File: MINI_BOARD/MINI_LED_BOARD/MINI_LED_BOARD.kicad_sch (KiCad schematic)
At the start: 38 parts, among them J1 Conn_ARM_SWD_TagConnect_TC2030, J2 430450428, U1 MSPM0C1103SDDFR, U2 TCAN334, U4 TPS76333DBVR

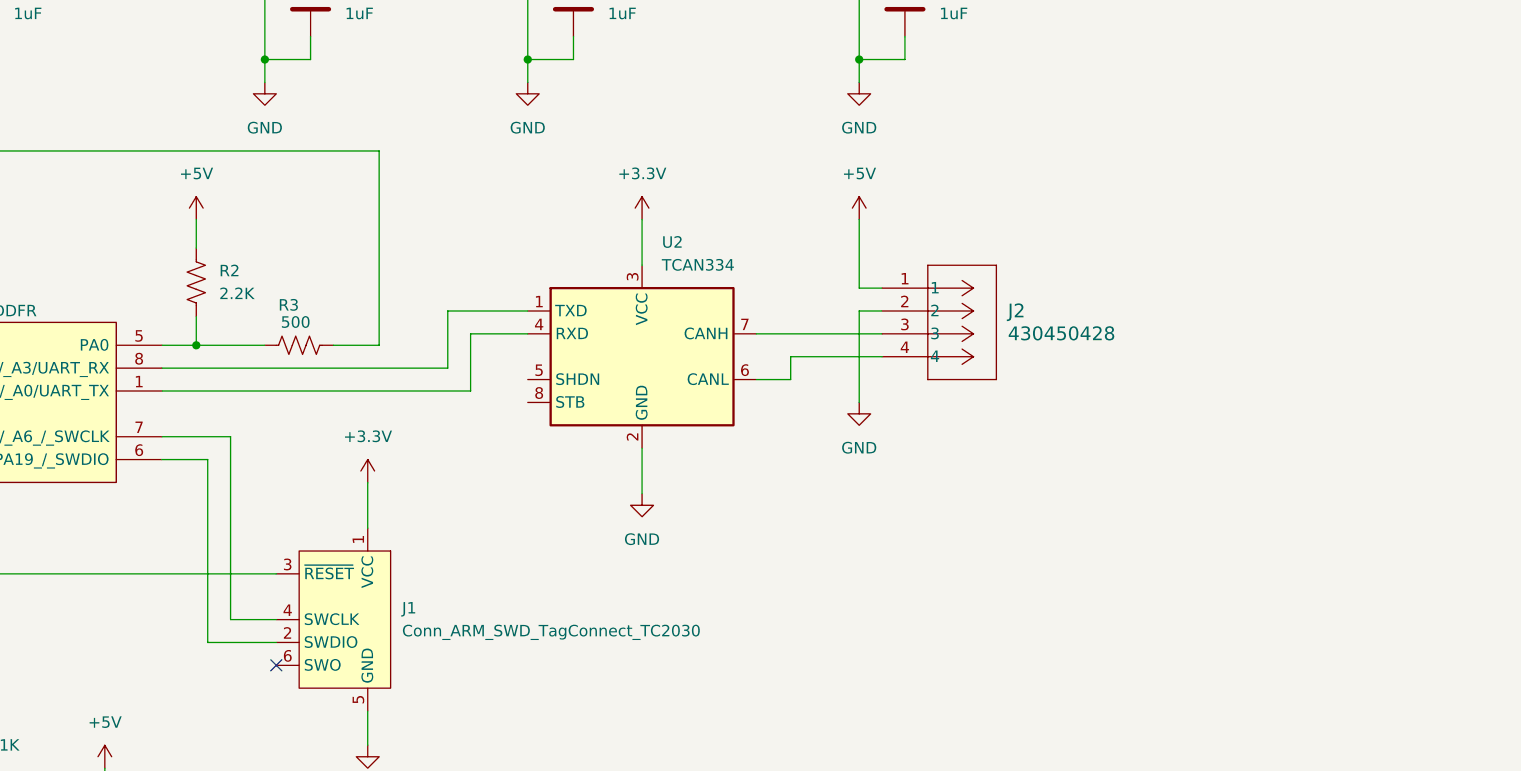
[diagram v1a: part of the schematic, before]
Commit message: Add more TCAN passives and mess with layout
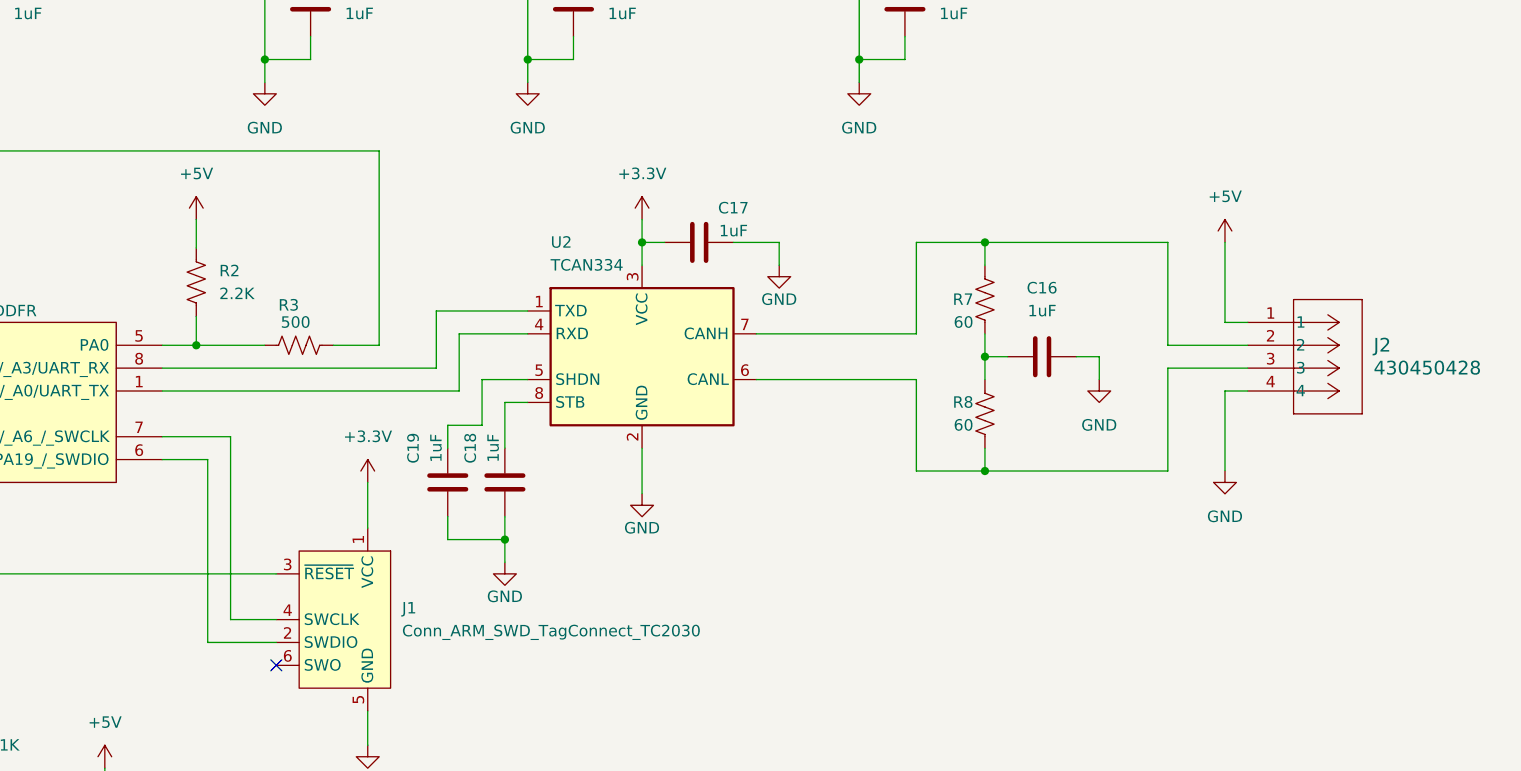
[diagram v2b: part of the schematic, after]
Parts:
- added C16, C17, C18, C19: 1uF, Capacitor_SMD:C_0603_1608Metric_Pad1.08x0.95mm_HandSolder, symbol Device:C
- added R7, R8: 60, Resistor_SMD:R_0603_1608Metric_Pad0.98x0.95mm_HandSolder, symbol Device:R_US
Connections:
- net +3.3V: now also C17.2
- net GND: now also J2.4, C16.2, C17.1, C18.2, C19.2; no longer J2.2
- net at U2.7 (CANH): now also J2.2, R7.2; no longer J2.3
- net at U2.6 (CANL): now also J2.3, R8.1; no longer J2.4
- net at U2.5 (SHDN): now also C19.1
- net at U2.8 (STB): now also C18.1
- new net: C16.1, R7.1, R8.2
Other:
- moved on the sheet: J2

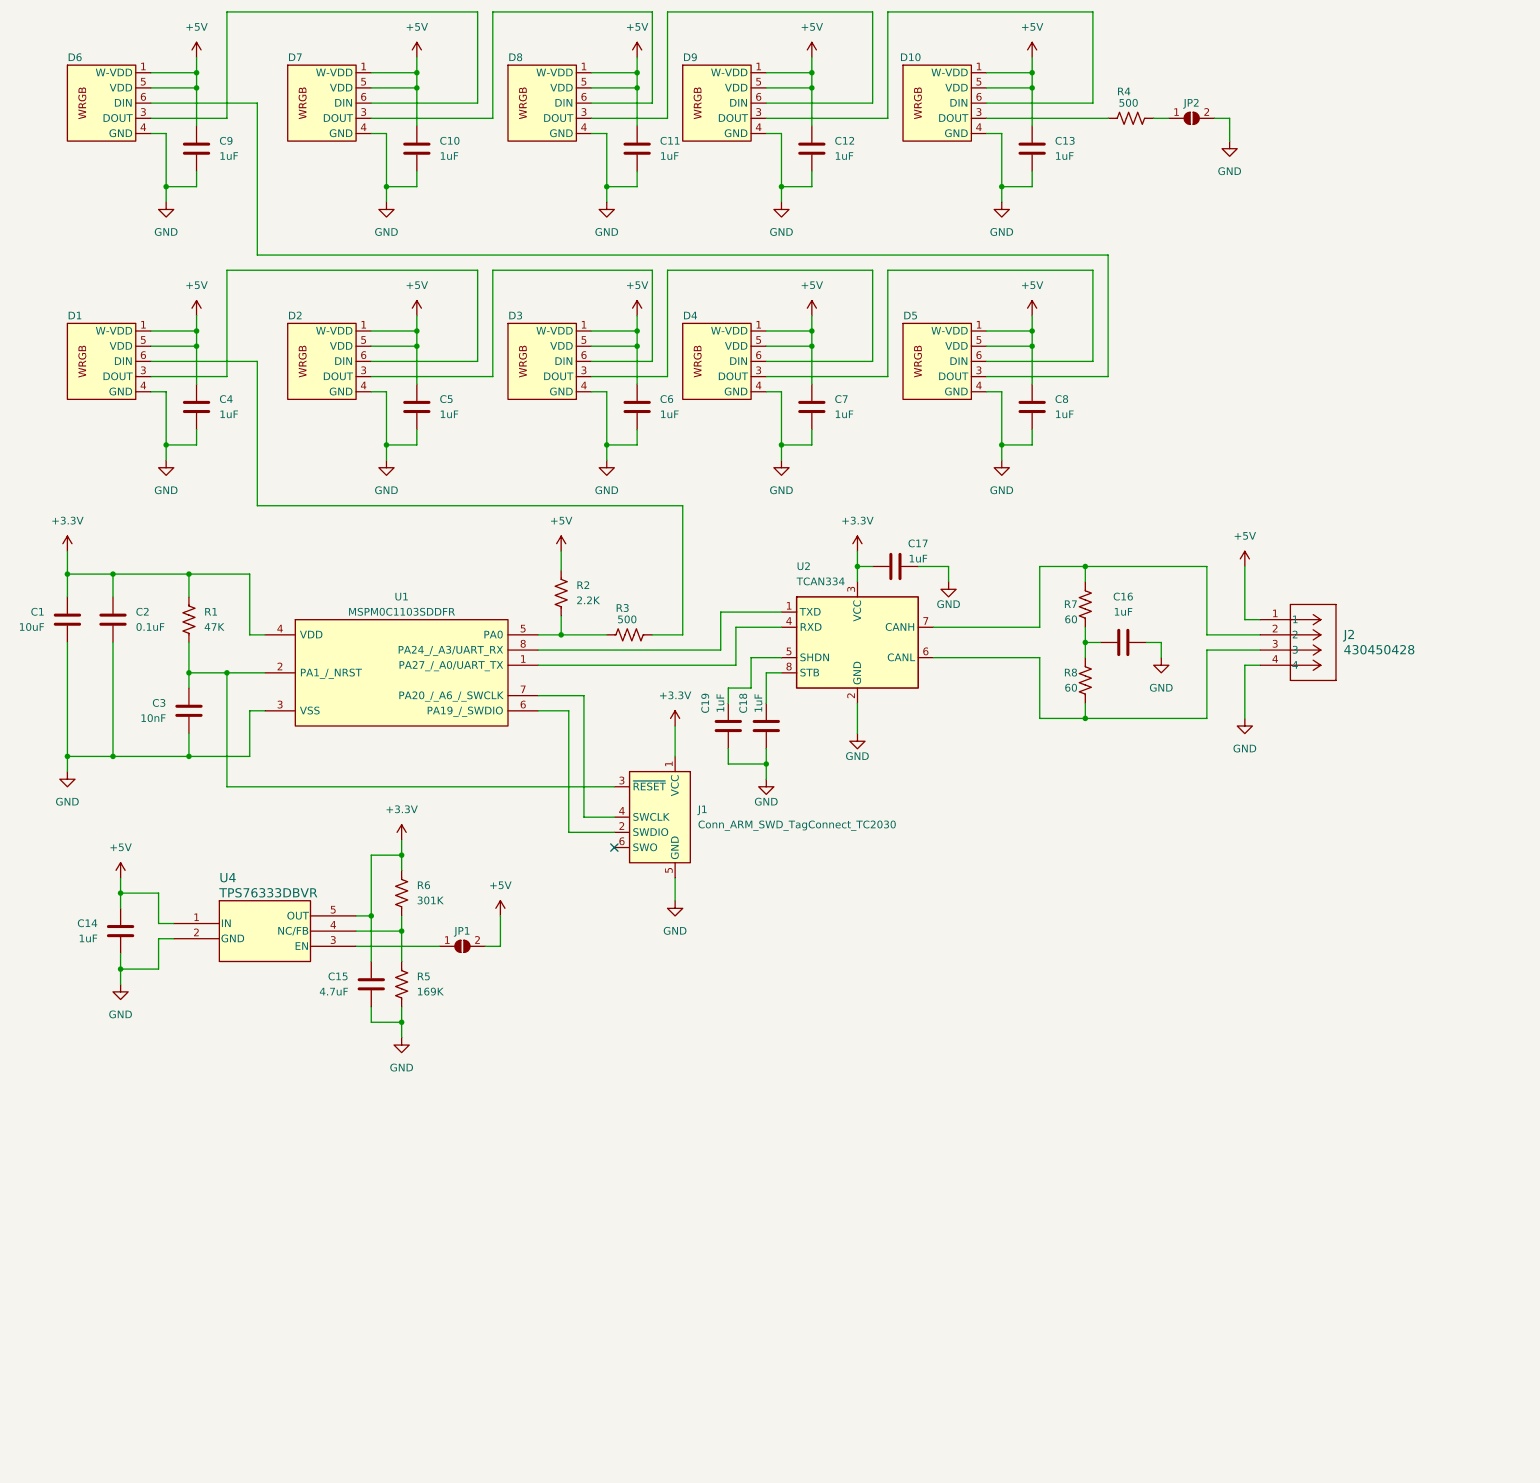
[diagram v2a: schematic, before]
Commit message: Finalize layout and conenction features; begin routing
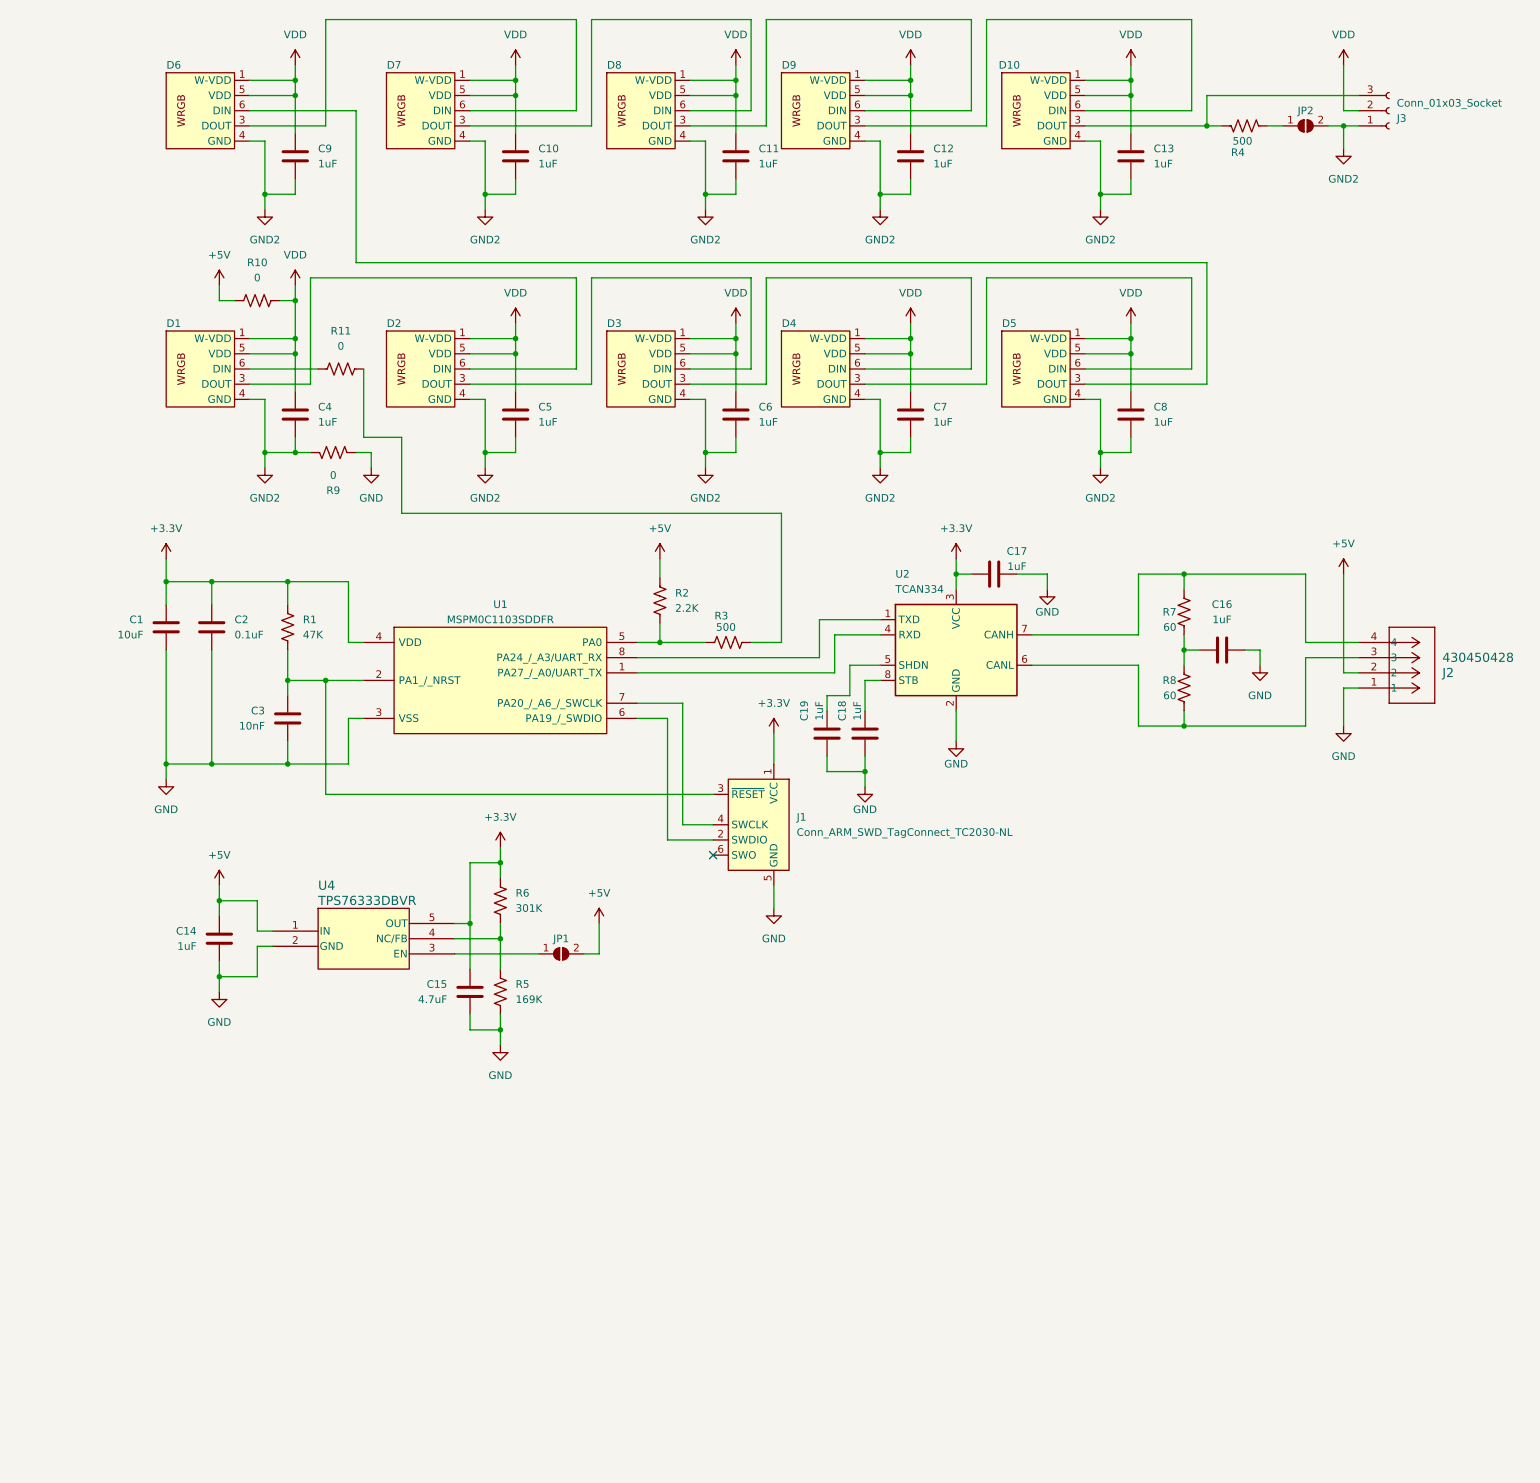
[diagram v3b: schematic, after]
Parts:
- removed J1: Conn_ARM_SWD_TagConnect_TC2030, Connector:Tag-Connect_TC2030-IDC-FP_2x03_P1.27mm_Vertical, symbol Connector:Conn_ARM_SWD_TagConnect_TC2030
- added J1: Conn_ARM_SWD_TagConnect_TC2030-NL, Connector:Tag-Connect_TC2030-IDC-NL_2x03_P1.27mm_Vertical, symbol Connector:Conn_ARM_SWD_TagConnect_TC2030-NL
- added J3: Conn_01x03_Socket, Connector_PinHeader_1.00mm:PinHeader_1x03_P1.00mm_Vertical, symbol Connector:Conn_01x03_Socket
- added R10, R11, R9: 0, Resistor_SMD:R_0603_1608Metric_Pad0.98x0.95mm_HandSolder, symbol Device:R_US
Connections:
- net +3.3V: now also J1.1 (VCC)
- net +5V: now also J2.2, R10.1; no longer C10.1, C11.1, C12.1, C13.1, C4.1, C5.1, C6.1, C7.1, C8.1, C9.1, D1.1 (W-VDD), D1.5 (VDD), D10.1 (W-VDD), D10.5 (VDD), D2.1 (W-VDD), D2.5 (VDD), D3.1 (W-VDD), D3.5 (VDD), D4.1 (W-VDD), D4.5 (VDD), D5.1 (W-VDD), D5.5 (VDD), D6.1 (W-VDD), D6.5 (VDD), D7.1 (W-VDD), D7.5 (VDD), D8.1 (W-VDD), D8.5 (VDD), D9.1 (W-VDD), D9.5 (VDD), J2.1
- net GND: now also J2.1, J1.5 (GND), R9.2; no longer C10.2, C11.2, C12.2, C13.2, C4.2, C5.2, C6.2, C7.2, C8.2, C9.2, D1.4 (GND), D10.4 (GND), D2.4 (GND), D3.4 (GND), D4.4 (GND), D5.4 (GND), D6.4 (GND), D7.4 (GND), D8.4 (GND), D9.4 (GND), J2.4, JP2.2 (B)
- net at C3.1, R1.2, U1.2 (PA1_/_NRST): now also J1.3 (~{RESET})
- net at U1.6 (PA19_/_SWDIO): now also J1.2 (SWDIO)
- net at U1.7 (PA20_/_A6_/_SWCLK): now also J1.4 (SWCLK)
- net at R7.2, U2.7 (CANH): now also J2.4; no longer J2.2
- net at D1.6 (DIN): now also R11.1; no longer R3.2
- net at D10.3 (DOUT), R4.1: now also J3.3 (Pin_3)
- new net: R11.2, R3.2
- new net GND2: C10.2, C11.2, C12.2, C13.2, C4.2, C5.2, C6.2, C7.2, C8.2, C9.2, D1.4 (GND), D10.4 (GND), D2.4 (GND), D3.4 (GND), D4.4 (GND), D5.4 (GND), D6.4 (GND), D7.4 (GND), D8.4 (GND), D9.4 (GND), J3.1 (Pin_1), JP2.2 (B), R9.1
- new net VDD: C10.1, C11.1, C12.1, C13.1, C4.1, C5.1, C6.1, C7.1, C8.1, C9.1, D1.1 (W-VDD), D1.5 (VDD), D10.1 (W-VDD), D10.5 (VDD), D2.1 (W-VDD), D2.5 (VDD), D3.1 (W-VDD), D3.5 (VDD), D4.1 (W-VDD), D4.5 (VDD), D5.1 (W-VDD), D5.5 (VDD), D6.1 (W-VDD), D6.5 (VDD), D7.1 (W-VDD), D7.5 (VDD), D8.1 (W-VDD), D8.5 (VDD), D9.1 (W-VDD), D9.5 (VDD), J3.2 (Pin_2), R10.2
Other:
- moved on the sheet: C1, C10, C11, C12, C13, C14, C15, C16, C17, C18, C19, C2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

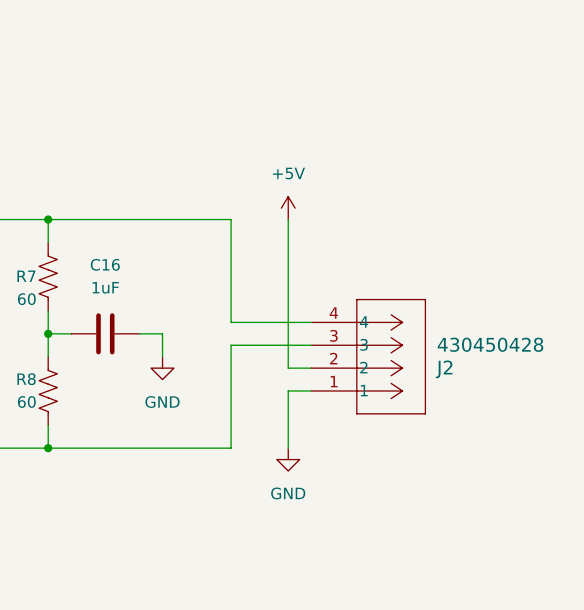
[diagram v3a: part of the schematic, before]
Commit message: Complete MCU side routing
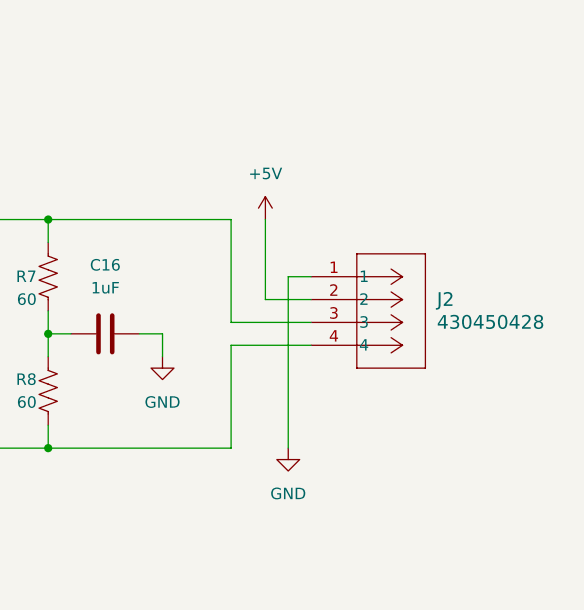
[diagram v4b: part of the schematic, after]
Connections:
- net at R8.1, U2.6 (CANL): now also J2.4; no longer J2.3
- net at R7.2, U2.7 (CANH): now also J2.3; no longer J2.4
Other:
- moved on the sheet: J2
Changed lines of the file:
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@@
     (stroke (width 0) (type default))
   )
-  (wire (pts (xy 237.49 130.81) (xy 240.03 130.81))
+  (wire (pts (xy 237.49 118.11) (xy 240.03 118.11))
     (stroke (width 0) (type default))
   )
@@
     (stroke (width 0) (type default))
   )
-  (wire (pts (xy 237.49 128.27) (xy 240.03 128.27))
+  (wire (pts (xy 234.95 120.65) (xy 240.03 120.65))
     (stroke (width 0) (type default))
   )
@@
     (stroke (width 0) (type default))
   )
-  (wire (pts (xy 237.49 128.27) (xy 237.49 111.76))
+  (wire (pts (xy 234.95 120.65) (xy 234.95 111.76))
     (stroke (width 0) (type default))
   )
@@
     (stroke (width 0) (type default))
   )
-  (wire (pts (xy 237.49 130.81) (xy 237.49 137.16))
+  (wire (pts (xy 237.49 118.11) (xy 237.49 137.16))
     (stroke (width 0) (type default))
   )
@@
     )
   )
-  (symbol (lib_id "430450428:430450428") (at 240.03 130.81 0) (mirror x) (unit 1)
+  (symbol (lib_id "430450428:430450428") (at 240.03 118.11 0) (unit 1)
     (in_bom yes) (on_board yes) (dnp no)
-    (property "Reference" "J2" (at 254 128.27 0)
+    (property "Reference" "J2" (at 254 120.65 0)
       (effects (font (size 1.524 1.524)) (justify left))
     )
-    (property "Value" "430450428" (at 254 125.73 0)
+    (property "Value" "430450428" (at 254 123.19 0)
       (effects (font (size 1.524 1.524)) (justify left))
     )
-    (property "Footprint" "430450428:CON_430450428_MOL" (at 240.03 130.81 0)
+    (property "Footprint" "430450428:CON_430450428_MOL" (at 240.03 118.11 0)
       (effects (font (size 1.27 1.27) italic) hide)
     )
-    (property "Datasheet" "430450428" (at 240.03 130.81 0)
+    (property "Datasheet" "430450428" (at 240.03 118.11 0)
       (effects (font (size 1.27 1.27) italic) hide)
     )
@@
     )
   )
-  (symbol (lib_id "power:+5V") (at 237.49 111.76 0) (unit 1)
-    (in_bom yes) (on_board yes) (dnp no) (fields_autoplaced)
-    (property "Reference" "#PWR017" (at 237.49 115.57 0)
-      (effects (font (size 1.27 1.27)) hide)
-    )
-    (property "Value" "+5V" (at 237.49 106.68 0)
-      (effects (font (size 1.27 1.27)))
-    )
-    (property "Footprint" "" (at 237.49 111.76 0)
-      (effects (font (size 1.27 1.27)) hide)
-    )
-    (property "Datasheet" "" (at 237.49 111.76 0)
-      (effects (font (size 1.27 1.27)) hide)
-    )
+  (symbol (lib_id "power:+5V") (at 234.95 111.76 0) (unit 1)
+    (in_bom yes) (on_board yes) (dnp no) (fields_autoplaced)
+    (property "Reference" "#PWR017" (at 234.95 115.57 0)
+      (effects (font (size 1.27 1.27)) hide)
+    )
+    (property "Value" "+5V" (at 234.95 106.68 0)
+      (effects (font (size 1.27 1.27)))
+    )
+    (property "Footprint" "" (at 234.95 111.76 0)
+      (effects (font (size 1.27 1.27)) hide)
+    )
+    (property "Datasheet" "" (at 234.95 111.76 0)
+      (effects (font (size 1.27 1.27)) hide)
+    )
